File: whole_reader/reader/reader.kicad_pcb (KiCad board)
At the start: 2 copper layers, 50 x 58.5 mm, 66 parts, among them U1 LM386, U2 STM32F103C8T6, U3 MCP16301Hx-xCH, U4 MAX3232, Y1 16MHz

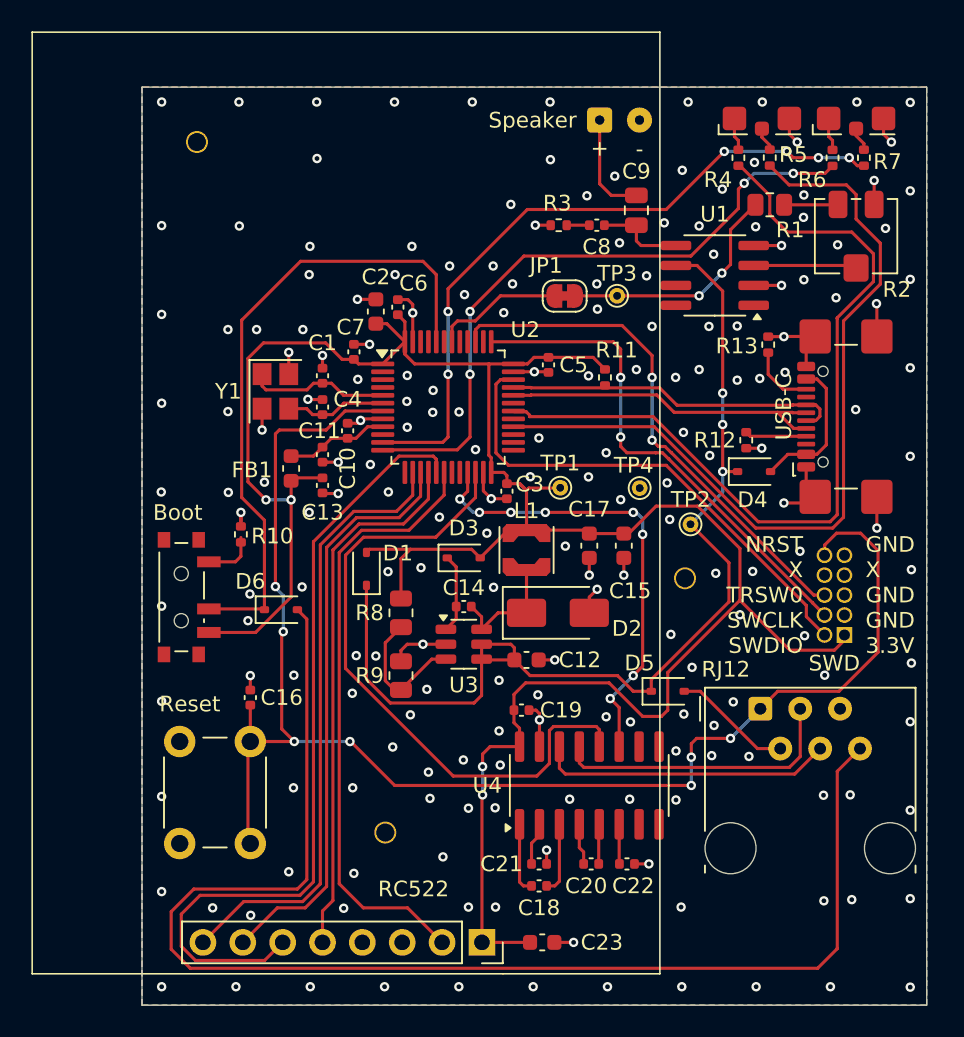
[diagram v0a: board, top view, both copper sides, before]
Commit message: Netclass Power and GND track width set to 3.0 mm
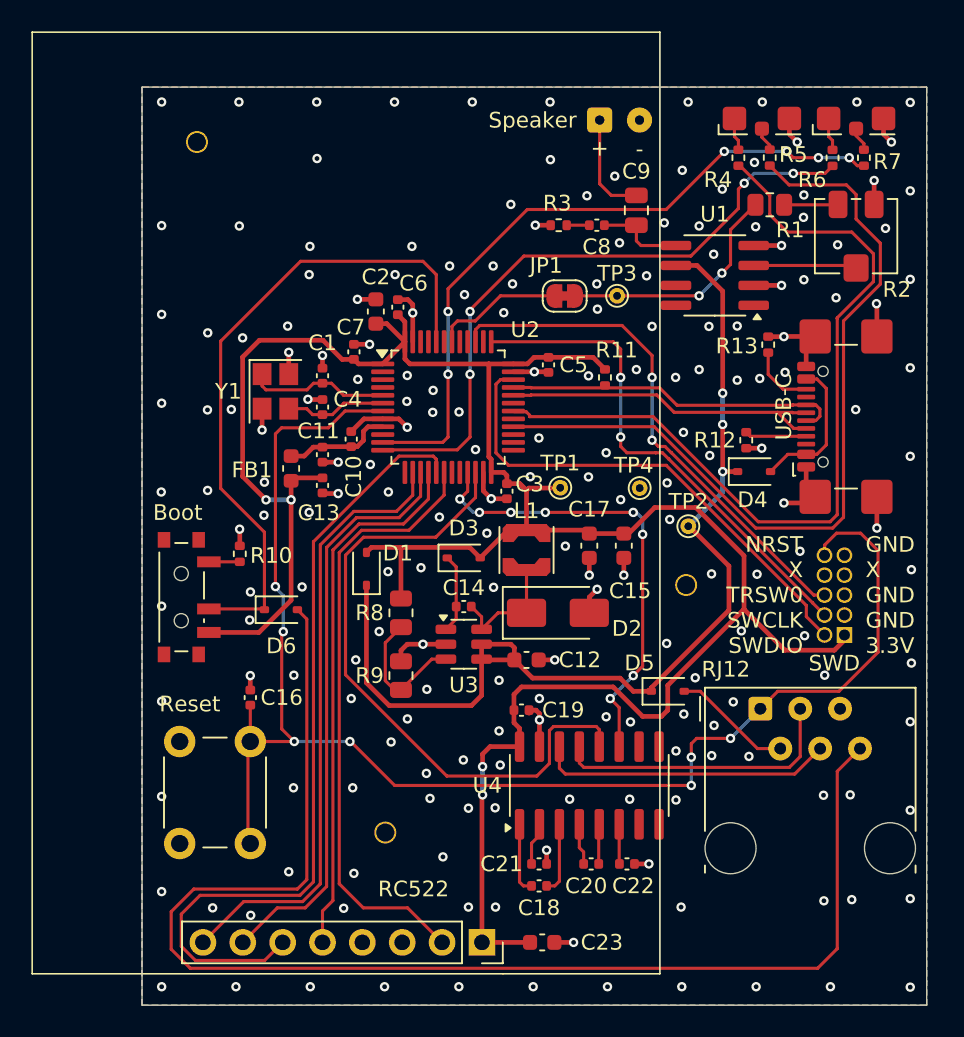
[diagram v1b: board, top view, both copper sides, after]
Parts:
- moved R10 1.24 mm to (138.7, 57.2)
- moved C10 0.58 mm to (145.8, 49.9)
- moved H2 0.44 mm to (167.2, 59.2)
- moved TP2 0.18 mm to (167.3, 55.5)
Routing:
- net GND: track 57.2 -> 58.8 mm, vias 200 -> 201
- net Net-(BOOT1-A): track 3.38 -> 1.97 mm
- net BOOT0: track 41.1 -> 42.2 mm

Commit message: Rozšírenie GND výplne na niektorých miestach
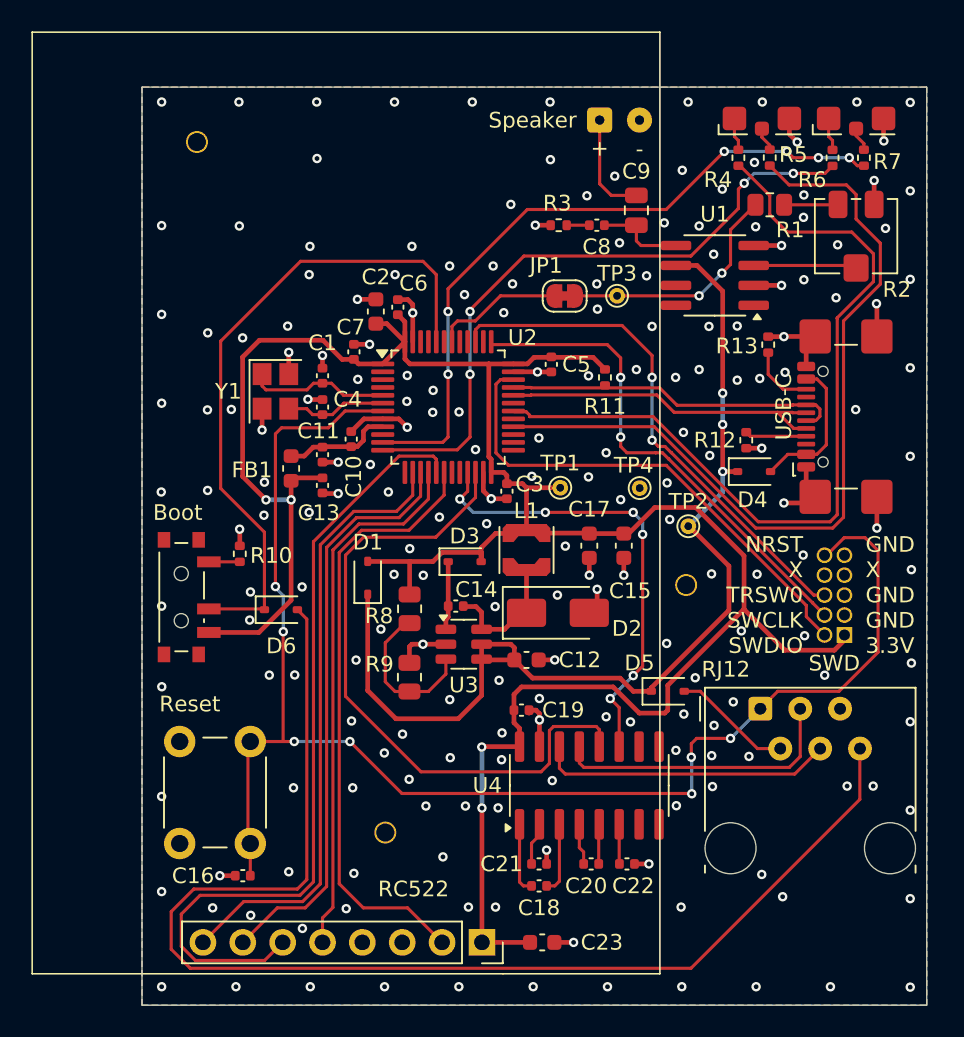
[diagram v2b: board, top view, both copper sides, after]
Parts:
- moved C16 11.4 mm to (138.9, 77.8), turned to 180 degrees
- moved R8 0.61 mm to (149.6, 60.7)
- moved D1 0.58 mm to (146.9, 58.8)
- moved R9 0.55 mm to (149.5, 65.1)
- moved C14 0.51 mm to (152.5, 60.6)
- moved D3 0.25 mm to (153.1, 57.7)
- moved C5 0.18 mm to (158.6, 45.2)
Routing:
- net Net-(D6-A): track 86.1 -> 81.4 mm
- net Net-(U3-Vfb): track 8.33 -> 9.42 mm
- net GND: track 58.8 -> 57.8 mm, vias 201 -> 205
- net NRST: track 94.3 -> 93.5 mm
- net Net-(D3-K): track 5.06 -> 4.29 mm
- net USART3_RX: track 41.2 -> 41.8 mm
- net USART3_TX: track 29.7 -> 29.6 mm, vias 8 -> 6

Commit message: Pridanie slzičiek
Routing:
- net GND: track 57.8 -> 59.4 mm

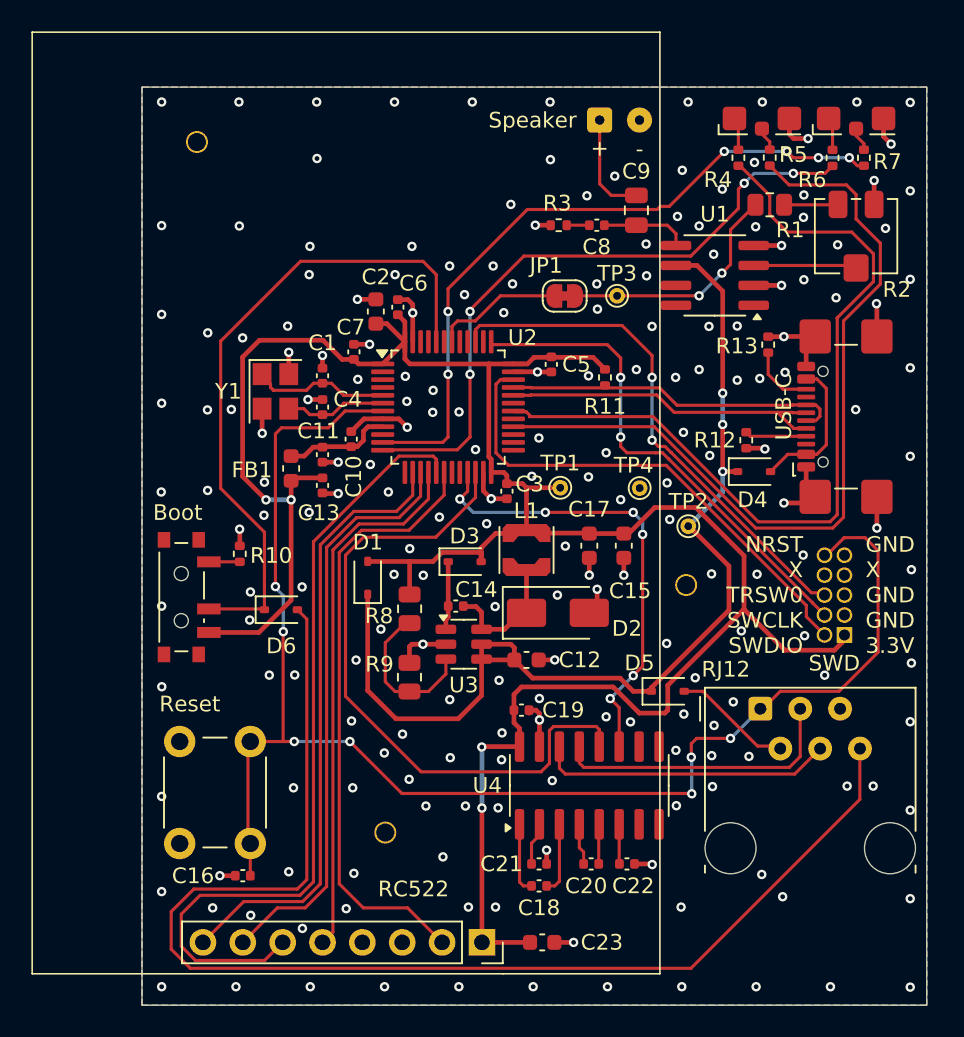
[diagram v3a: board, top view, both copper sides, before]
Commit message: Úprava GND výplne, netclass a šírky niektorých spojov
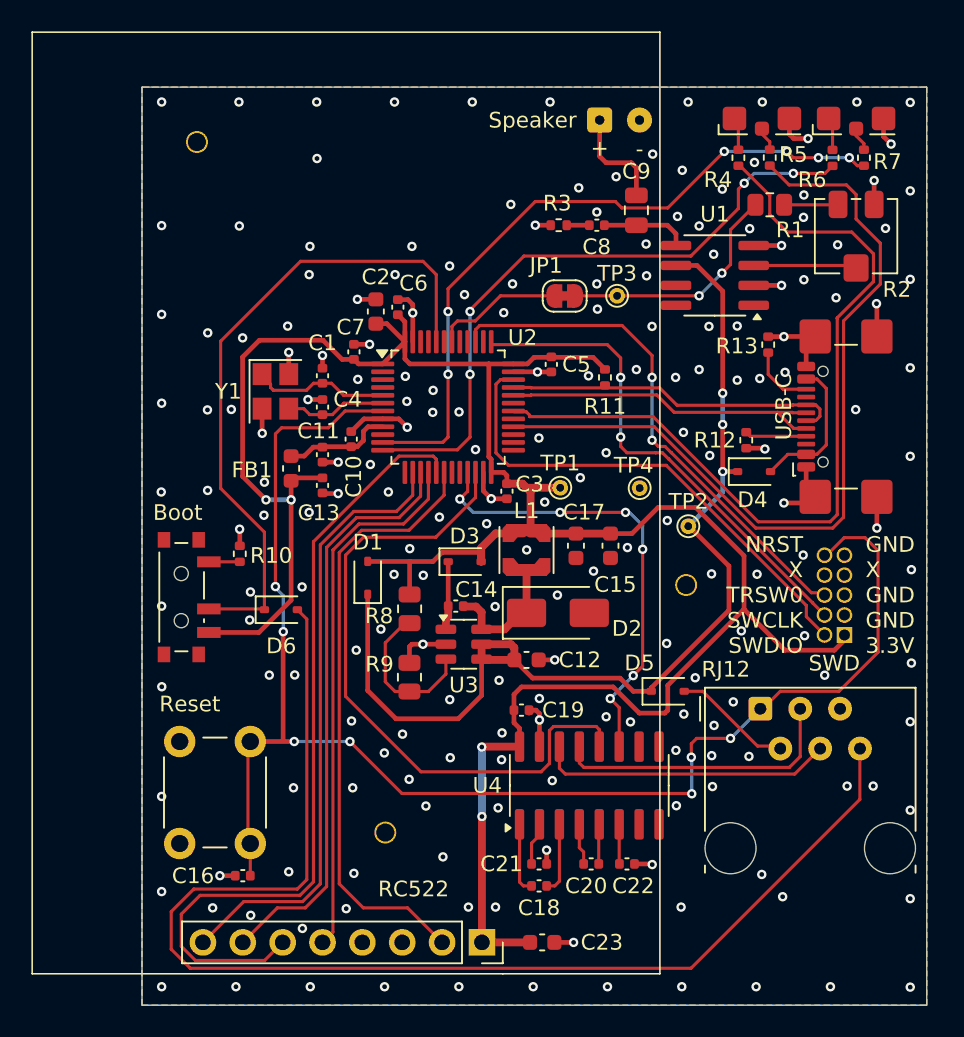
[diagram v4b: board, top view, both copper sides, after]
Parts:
- moved C15 0.85 mm to (162.3, 56.7)
- moved C17 0.85 mm to (160.2, 56.7)
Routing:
- net GND: track 59.4 -> 56.5 mm, vias 205 -> 201
- net +3.3V: track 153.2 -> 153.8 mm

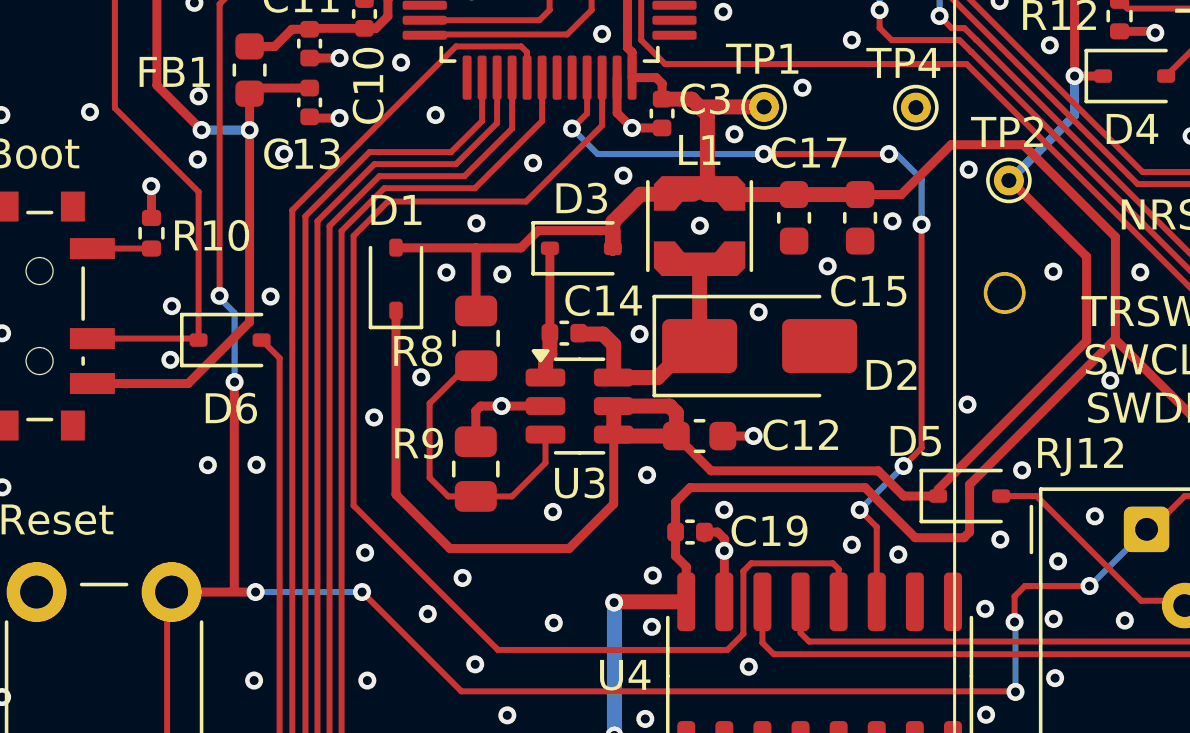
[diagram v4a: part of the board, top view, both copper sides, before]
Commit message: changed diodes
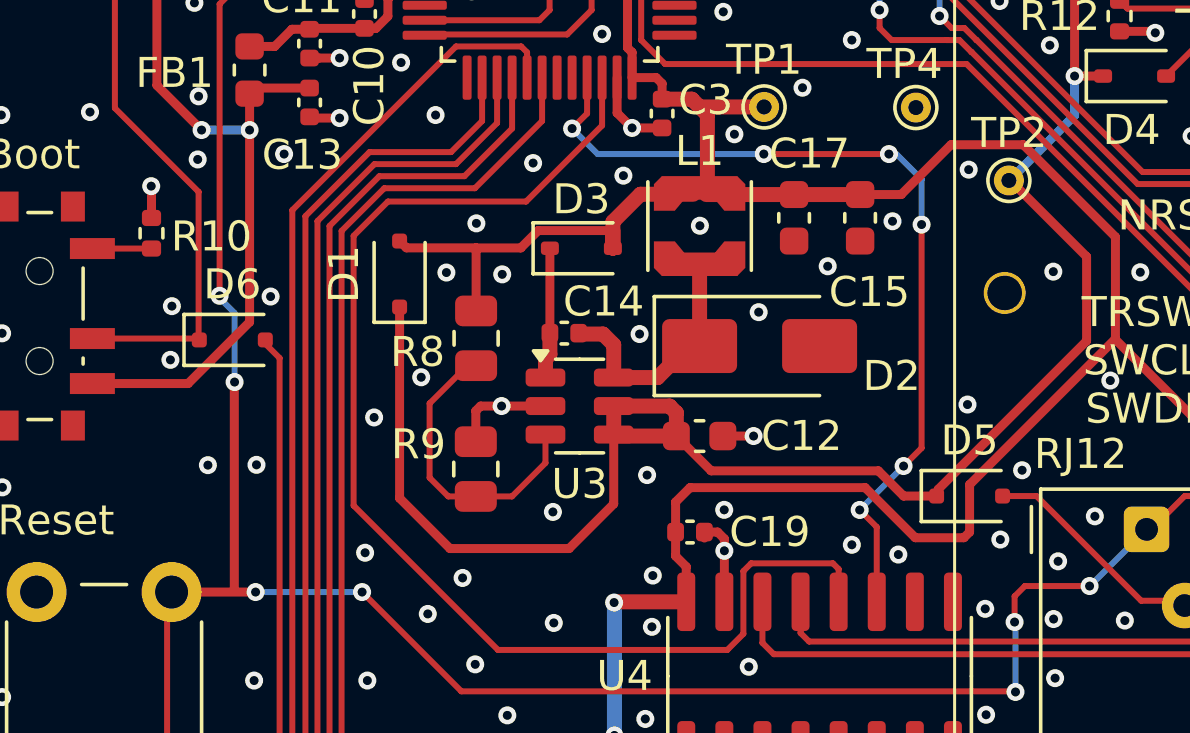
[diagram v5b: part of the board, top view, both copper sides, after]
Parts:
- D1, D5, D6: value BAT60A -> BAT54J; footprint Diode_SMD:D_SOD-323 -> Diode_SMD:D_SOD-323F
- moved D1 0.21 mm to (147.0, 58.6)
- moved D6 0.07 mm to (141.4, 60.8)

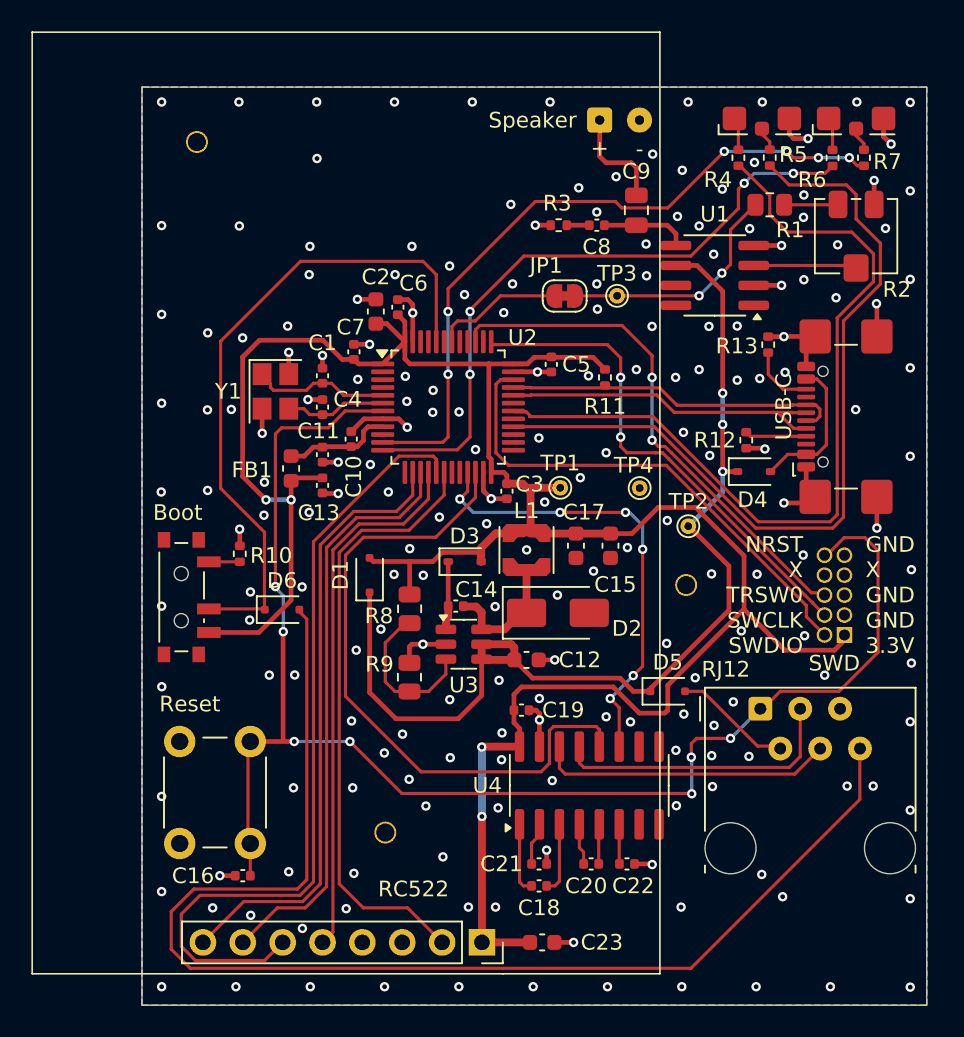
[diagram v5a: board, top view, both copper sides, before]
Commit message: added new diodes
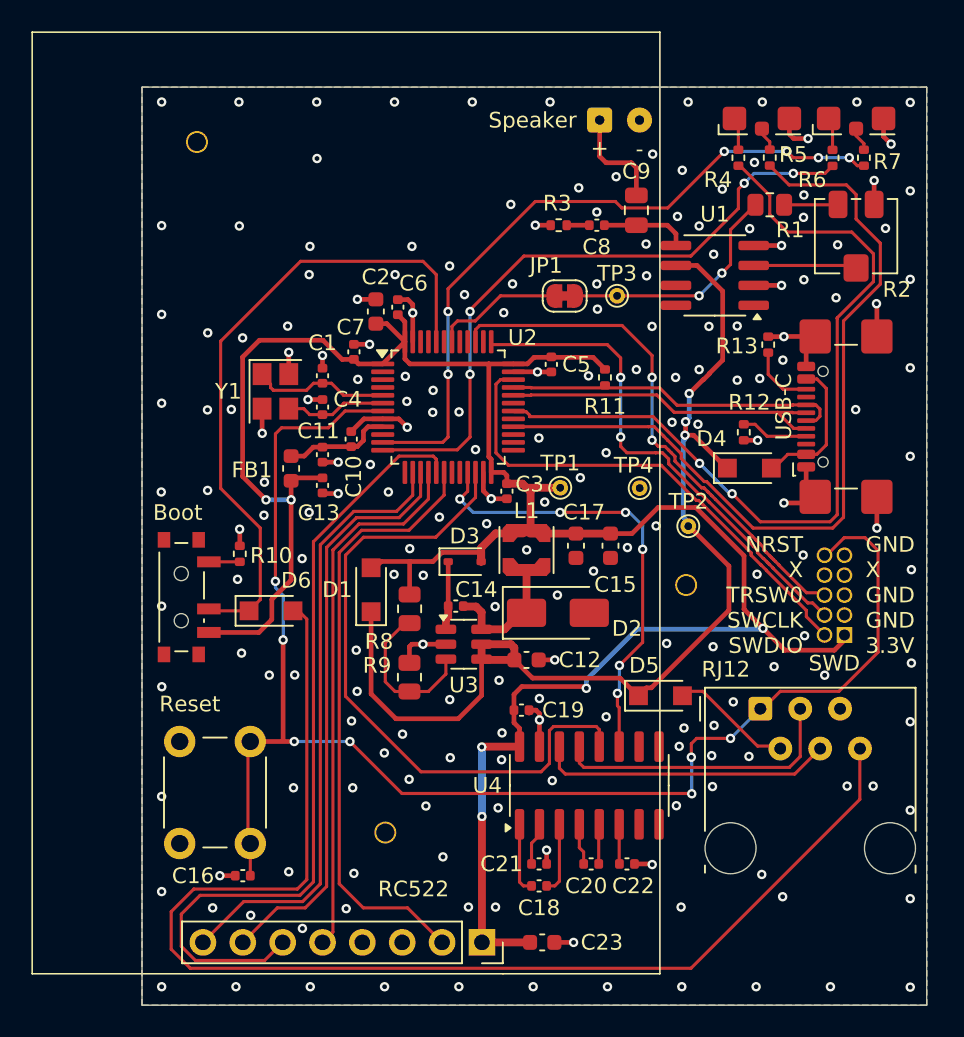
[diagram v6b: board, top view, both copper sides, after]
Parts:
- D1, D5, D6: value BAT54J -> PMEG2010ER; footprint Diode_SMD:D_SOD-323F -> Diode_SMD:Nexperia_CFP3_SOD-123W
- D4: value BAT60A -> PMEG2010ER; footprint Diode_SMD:D_SOD-323 -> Diode_SMD:Nexperia_CFP3_SOD-123W
- U1: value LM386 -> LM386M-1
- moved D1 0.93 mm to (147.1, 59.5)
- moved D6 0.71 mm to (140.7, 60.9)
- moved D5 0.54 mm to (165.5, 66.3)
- moved R12 0.53 mm to (170.8, 49.5)
- moved D4 0.37 mm to (171.2, 51.8)
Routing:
- net V+: track 66.4 -> 68.1 mm
- net +3.3V: track 153.9 -> 152.8 mm, vias 4 -> 6
- net BOOT0: track 42.2 -> 41.6 mm
- net GND: track 56.5 -> 56.2 mm, vias 201 -> 199
- net LED_R1: track 52.9 -> 52.8 mm, vias 0 -> 2
